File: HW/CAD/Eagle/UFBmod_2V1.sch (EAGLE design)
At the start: 192 parts, among them T0551 MMBT2222, U0501 MIDAS_MCCOG21605B6W-FPTLWI, U0601 MAX5217, U0701 AT86RF215-ZU, U0711 ASVTX-13-D-26.000MHZ-I05-T, U0811 PE4259, U0821 RFX1010, U0881 B39871B3440U410, U0911 FT232HL, U1101 TPS53353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

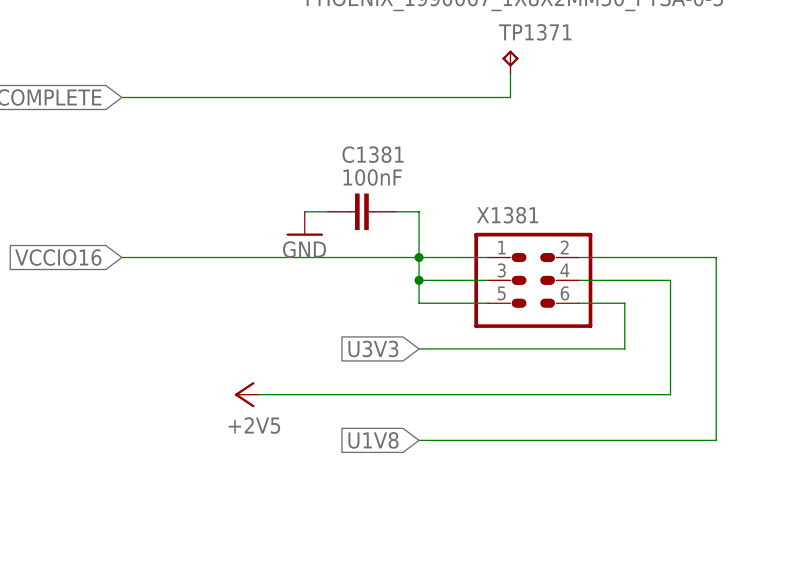
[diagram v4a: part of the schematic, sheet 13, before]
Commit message: HW - Eagle - V2.1 info added to use 3.3V @ bank 16
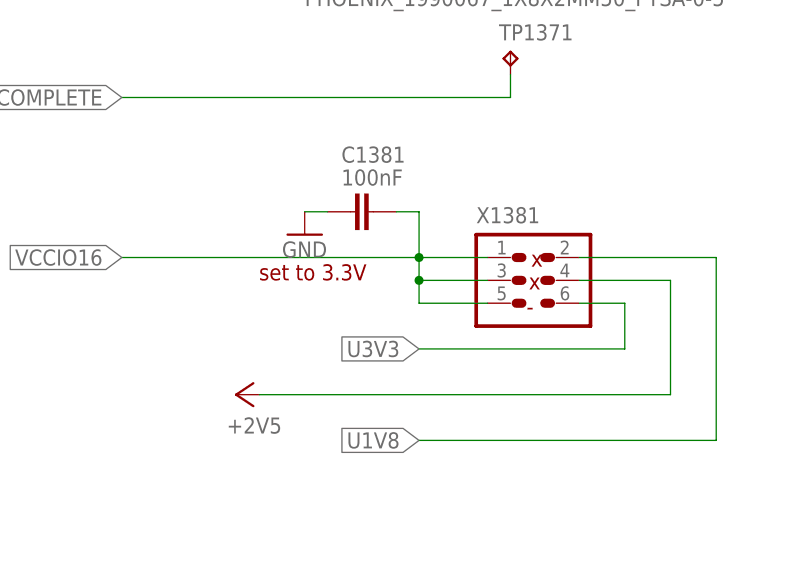
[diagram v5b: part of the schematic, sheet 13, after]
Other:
- note added: "-"
- note added: "set to 3.3V"
- note added: "x"
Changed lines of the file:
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@@
 <text x="15.24" y="96.52" size="1.778" layer="97">Programmer:
 Digilent JTAG HS3</text>
+<text x="193.04" y="55.88" size="1.778" layer="94">set to 3.3V</text>
+<text x="223.266" y="57.404" size="1.778" layer="94">x</text>
+<text x="223.012" y="54.864" size="1.778" layer="94">x</text>
+<text x="222.758" y="52.07" size="1.778" layer="94">-</text>
 </plain>
 <instances>

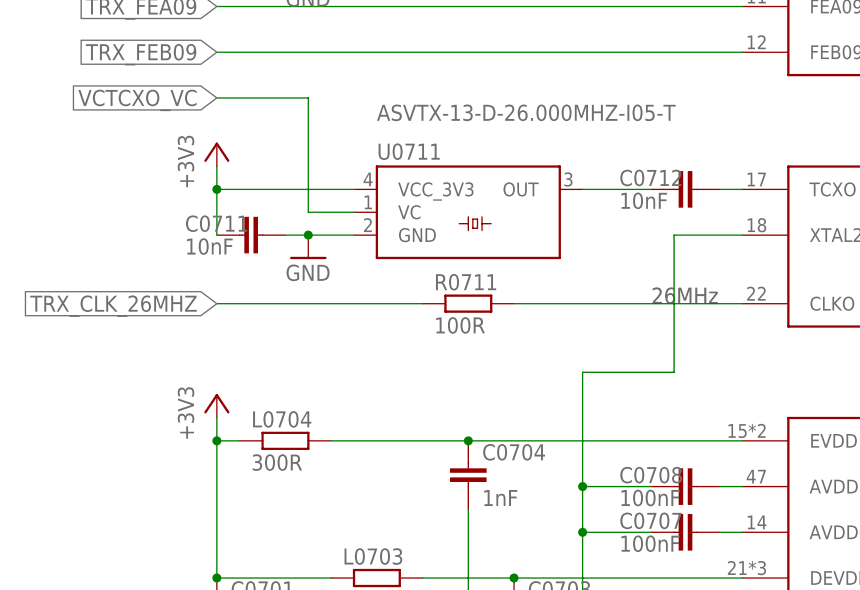
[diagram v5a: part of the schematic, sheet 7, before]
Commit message: HW - Eagle - V2.1 clock loop-back from FPGA out to extPLL in added
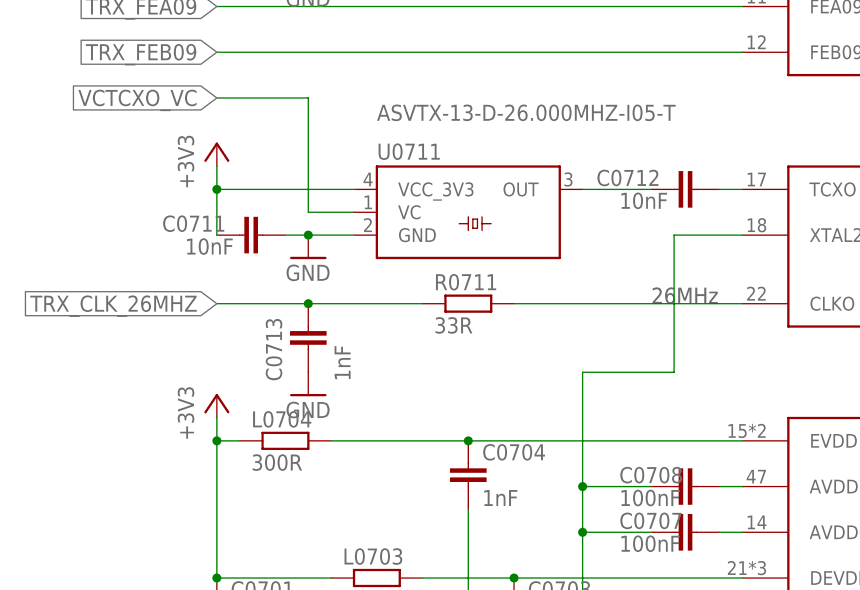
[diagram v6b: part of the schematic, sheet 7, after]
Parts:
- added C0713: 1nF, df4iah_rcl:C-EUC0402
- R0711: value 100R -> 33R
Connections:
- new net CLKIN2_N: JB3.B13_L16_N, JB3.CLKIN2_CLK_N
- new net CLKIN2_P: JB3.B13_L16_P, JB3.CLKIN2_CLK_P
- net GND: now also C0713.1
- net TRX_CLK_26MHZ: now also C0713.2
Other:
- note added: "25 MHz"
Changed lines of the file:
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@@
 <part name="S1321" library="df4iah_switch" deviceset="KSR223G_SMD_1POL" device=""/>
 <part name="R1321" library="df4iah_rcl" deviceset="R-EU_" device="R0402" value="1kR"/>
-<part name="R0711" library="df4iah_rcl" deviceset="R-EU_" device="R0402" value="100R"/>
+<part name="R0711" library="df4iah_rcl" deviceset="R-EU_" device="R0402" value="33R"/>
 <part name="C1321" library="df4iah_rcl" deviceset="C-EU" device="C0402" value="100nF"/>
 <part name="GND0001" library="df4iah_supply" deviceset="GND" device=""/>
+<part name="C0713" library="df4iah_rcl" deviceset="C-EU" device="C0402" value="1nF"/>
+<part name="GND0712" library="df4iah_supply" deviceset="GND" device=""/>
 </parts>
 <sheets>
@@
 <text x="22.86" y="27.94" size="2.54" layer="97" ratio="15">Module mount pads</text>
 <text x="147.32" y="124.46" size="1.778" layer="94" rot="R90">in</text>
+<text x="132.08" y="124.46" size="1.778" layer="94" rot="R90">in</text>
+<text x="134.62" y="124.46" size="1.778" layer="94" rot="R90">in</text>
+<text x="139.7" y="124.46" size="1.778" layer="94" rot="R90">out</text>
+<text x="142.24" y="124.46" size="1.778" layer="94" rot="R90">out</text>
+<text x="119.38" y="147.32" size="1.778" layer="94">25 MHz</text>
 </plain>
 <instances>
@@
 </segment>
 </net>
+<net name="CLKIN2_N" class="0">
+<segment>
+<pinref part="JB3" gate="G$1" pin="CLKIN2_CLK_N"/>
+<wire x1="132.08" y1="124.46" x2="132.08" y2="147.32" width="0.1524" layer="91"/>
+<wire x1="132.08" y1="147.32" x2="142.24" y2="147.32" width="0.1524" layer="91"/>
+<pinref part="JB3" gate="G$1" pin="B13_L16_N"/>
+<wire x1="142.24" y1="147.32" x2="142.24" y2="124.46" width="0.1524" layer="91"/>
+<label x="132.08" y="147.32" size="1.778" layer="95"/>
+</segment>
+</net>
+<net name="CLKIN2_P" class="0">
+<segment>
+<pinref part="JB3" gate="G$1" pin="CLKIN2_CLK_P"/>
+<wire x1="134.62" y1="124.46" x2="134.62" y2="142.24" width="0.1524" layer="91"/>
+<wire x1="134.62" y1="142.24" x2="139.7" y2="142.24" width="0.1524" layer="91"/>
+<pinref part="JB3" gate="G$1" pin="B13_L16_P"/>
+<wire x1="139.7" y1="142.24" x2="139.7" y2="124.46" width="0.1524" layer="91"/>
+<label x="132.08" y="142.24" size="1.778" layer="95"/>
+</segment>
+</net>
 </nets>
 </sheet>
@@
 </instance>
 <instance part="C0712" gate="G$1" x="96.52" y="96.52" smashed="yes" rot="R90">
-<attribute name="NAME" x="90.424" y="96.901" size="1.778" layer="95"/>
+<attribute name="NAME" x="87.884" y="96.901" size="1.778" layer="95"/>
 <attribute name="VALUE" x="90.424" y="94.361" size="1.778" layer="96"/>
 </instance>
@@
 <instance part="GND0711" gate="1" x="55.88" y="88.9"/>
 <instance part="C0711" gate="G$1" x="48.26" y="91.44" smashed="yes" rot="R90">
-<attribute name="NAME" x="42.164" y="91.821" size="1.778" layer="95"/>
+<attribute name="NAME" x="39.624" y="91.821" size="1.778" layer="95"/>
 <attribute name="VALUE" x="42.164" y="89.281" size="1.778" layer="96"/>
 </instance>
@@
 <instance part="R0754" gate="G$1" x="185.42" y="53.34"/>
 <instance part="R0711" gate="G$1" x="73.66" y="83.82"/>
+<instance part="C0713" gate="G$1" x="55.88" y="78.74" smashed="yes" rot="R180">
+<attribute name="NAME" x="52.959" y="75.184" size="1.778" layer="95" rot="R90"/>
+<attribute name="VALUE" x="60.579" y="75.184" size="1.778" layer="96" rot="R90"/>
+</instance>
+<instance part="GND0712" gate="1" x="55.88" y="73.66"/>
 </instances>
 <busses>
@@
 <wire x1="63.5" y1="142.24" x2="66.04" y2="142.24" width="0.1524" layer="91"/>
 </segment>
+<segment>
+<pinref part="C0713" gate="G$1" pin="1"/>
+<pinref part="GND0712" gate="1" pin="GND"/>
+</segment>
 </net>
 <net name="TRX_EVDD" class="0">
@@
 <segment>
 <pinref part="R0711" gate="G$1" pin="1"/>
-<wire x1="68.58" y1="83.82" x2="45.72" y2="83.82" width="0.1524" layer="91"/>
+<wire x1="68.58" y1="83.82" x2="55.88" y2="83.82" width="0.1524" layer="91"/>
 <label x="45.72" y="83.82" size="1.778" layer="95" rot="R180" xref="yes"/>
-</segment>
-</net>
+<pinref part="C0713" gate="G$1" pin="2"/>
+<wire x1="55.88" y1="83.82" x2="45.72" y2="83.82" width="0.1524" layer="91"/>
+<junction x="55.88" y="83.82"/>
+</segment>
+</net>

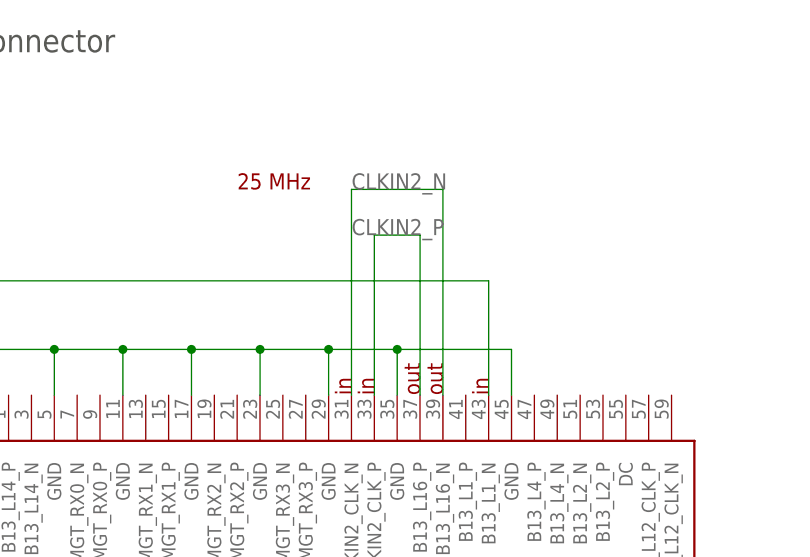
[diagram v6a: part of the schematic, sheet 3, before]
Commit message: HW - Eagle - V2.1 LVDS dummy output TXD[1] added
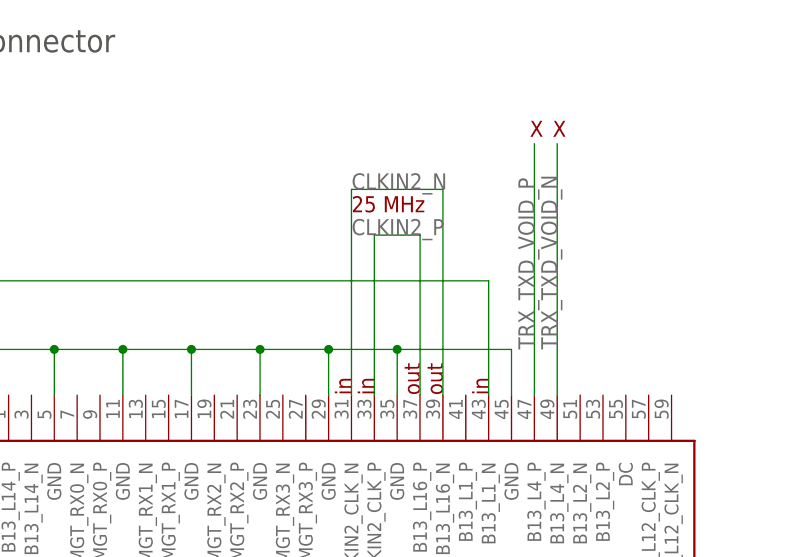
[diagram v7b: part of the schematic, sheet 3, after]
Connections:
- new net TRX_TXD_VOID_N: JB3.B13_L4_N
- new net TRX_TXD_VOID_P: JB3.B13_L4_P
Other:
- note added: "X"
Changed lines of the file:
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@@
 <text x="139.7" y="124.46" size="1.778" layer="94" rot="R90">out</text>
 <text x="142.24" y="124.46" size="1.778" layer="94" rot="R90">out</text>
-<text x="119.38" y="147.32" size="1.778" layer="94">25 MHz</text>
+<text x="132.08" y="144.78" size="1.778" layer="94">25 MHz</text>
+<text x="151.892" y="153.162" size="1.778" layer="94">X</text>
+<text x="154.432" y="153.162" size="1.778" layer="94">X</text>
 </plain>
 <instances>
@@
 </segment>
 </net>
+<net name="TRX_TXD_VOID_N" class="0">
+<segment>
+<pinref part="JB3" gate="G$1" pin="B13_L4_N"/>
+<wire x1="154.94" y1="124.46" x2="154.94" y2="152.4" width="0.1524" layer="91"/>
+<label x="154.94" y="129.54" size="1.778" layer="95" rot="R90"/>
+</segment>
+</net>
+<net name="TRX_TXD_VOID_P" class="0">
+<segment>
+<pinref part="JB3" gate="G$1" pin="B13_L4_P"/>
+<wire x1="152.4" y1="124.46" x2="152.4" y2="152.4" width="0.1524" layer="91"/>
+<label x="152.4" y="129.54" size="1.778" layer="95" rot="R90"/>
+</segment>
+</net>

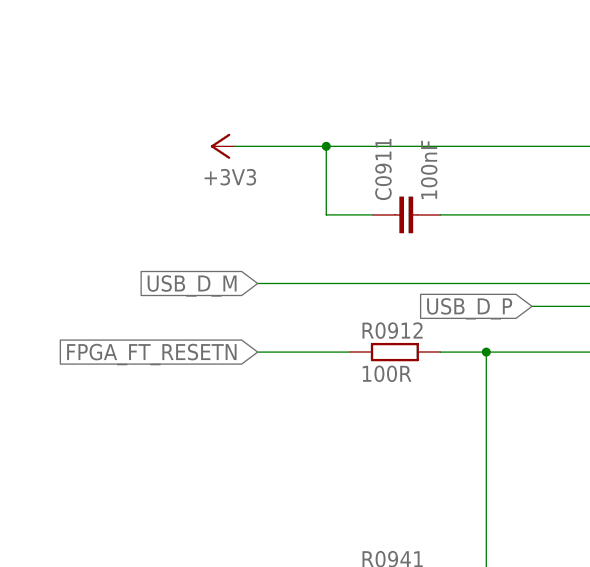
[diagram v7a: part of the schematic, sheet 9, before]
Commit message: HW_2V0 - CAD/Eagle - TRX frontend routed
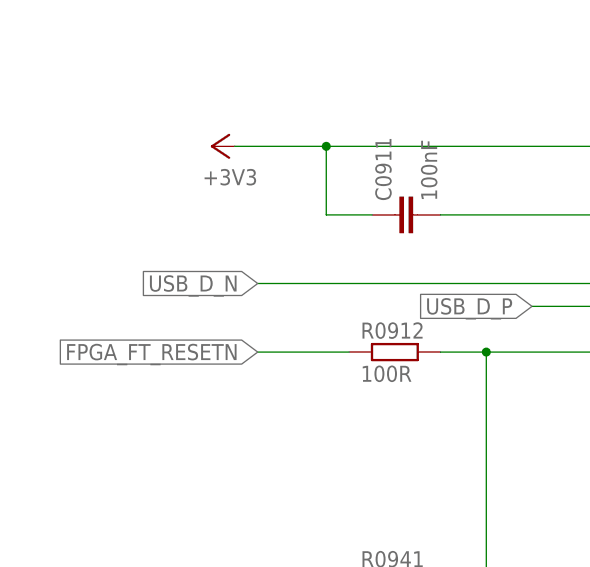
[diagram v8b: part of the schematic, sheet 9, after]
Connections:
- net USB_D_M renamed USB_D_N
- net BOARD_LCD_RESETN: now also JB1.B14_L4_MIO_N
- net DDR3_INIT_CALIB_COMPLETE: now also JB2.B14_L8_P
- net FPGA_LCD_BL_PWM: now also JB1.B14_L4_MIO_P
- net FPGA_LED_RGB_BLUE: now also JB1.B14_L24_MIO_N
- net FPGA_LED_RGB_GREEN: now also JB1.B14_L9_MIO_N
- net FPGA_LED_RGB_RED: now also JB1.B14_L9_MIO_P
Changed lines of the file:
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@@
 <wire x1="96.52" y1="38.1" x2="40.64" y2="38.1" width="0.1524" layer="91"/>
 <label x="40.64" y="38.1" size="1.778" layer="95" rot="R180" xref="yes"/>
+<pinref part="JB1" gate="G$1" pin="B14_L9_MIO_P"/>
 </segment>
 </net>
@@
 <wire x1="96.52" y1="35.56" x2="76.2" y2="35.56" width="0.1524" layer="91"/>
 <label x="76.2" y="35.56" size="1.778" layer="95" rot="R180" xref="yes"/>
+<pinref part="JB1" gate="G$1" pin="B14_L9_MIO_N"/>
 </segment>
 </net>
@@
 <wire x1="96.52" y1="27.94" x2="40.64" y2="27.94" width="0.1524" layer="91"/>
 <label x="40.64" y="27.94" size="1.778" layer="95" rot="R180" xref="yes"/>
+<pinref part="JB1" gate="G$1" pin="B14_L24_MIO_N"/>
 </segment>
 </net>
@@
 <wire x1="96.52" y1="33.02" x2="40.64" y2="33.02" width="0.1524" layer="91"/>
 <label x="40.64" y="33.02" size="1.778" layer="95" rot="R180" xref="yes"/>
+<pinref part="JB1" gate="G$1" pin="B14_L4_MIO_P"/>
 </segment>
 </net>
@@
 <wire x1="96.52" y1="30.48" x2="76.2" y2="30.48" width="0.1524" layer="91"/>
 <label x="76.2" y="30.48" size="1.778" layer="95" rot="R180" xref="yes"/>
+<pinref part="JB1" gate="G$1" pin="B14_L4_MIO_N"/>
 </segment>
 </net>
@@
 <wire x1="96.52" y1="137.16" x2="76.2" y2="137.16" width="0.1524" layer="91"/>
 <label x="76.2" y="137.16" size="1.778" layer="95" rot="R180" xref="yes"/>
+<pinref part="JB2" gate="G$1" pin="B14_L8_P"/>
 </segment>
 </net>
@@
 </segment>
 </net>
-<net name="USB_D_M" class="0">
+<net name="USB_D_N" class="3">
 <segment>
 <pinref part="U0911" gate="G$1" pin="D_M"/>
@@
 </segment>
 </net>
-<net name="USB_D_P" class="0">
+<net name="USB_D_P" class="3">
 <segment>
 <pinref part="U0911" gate="G$1" pin="D_P"/>
@@
 </segment>
 </net>
-<net name="USB_D_M" class="0">
+<net name="USB_D_N" class="3">
 <segment>
 <pinref part="X1311" gate="G$1" pin="J_D-"/>
@@
 </segment>
 </net>
-<net name="USB_D_P" class="0">
+<net name="USB_D_P" class="3">
 <segment>
 <pinref part="X1311" gate="G$1" pin="J_D+"/>
